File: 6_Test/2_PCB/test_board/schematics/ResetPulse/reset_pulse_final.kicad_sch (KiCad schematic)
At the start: 3 parts

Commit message: Corrections to schematic 11_20_24
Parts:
- U?: footprint D14 -> nor_gate:nor_gate_D14
- U?: value SN74HC74DR -> D_FF
- gave numbers to parts that had none: 1
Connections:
- net GND: now also U?.10 (L), U?.4 (K), U?.5 (C), U?.6 (D), U?.8 (E), U?.9 (F)
- net V_SUP: now also U?.1 (*1CLR), U?.10 (*2PRE), U?.13 (*2CLR), U?.4 (*1PRE)
- net at U?.3 (J): now also U?.11 (2CLK); no longer U?.12 (2D)
- net at U?.5 (1Q): now also U?.12 (2D)

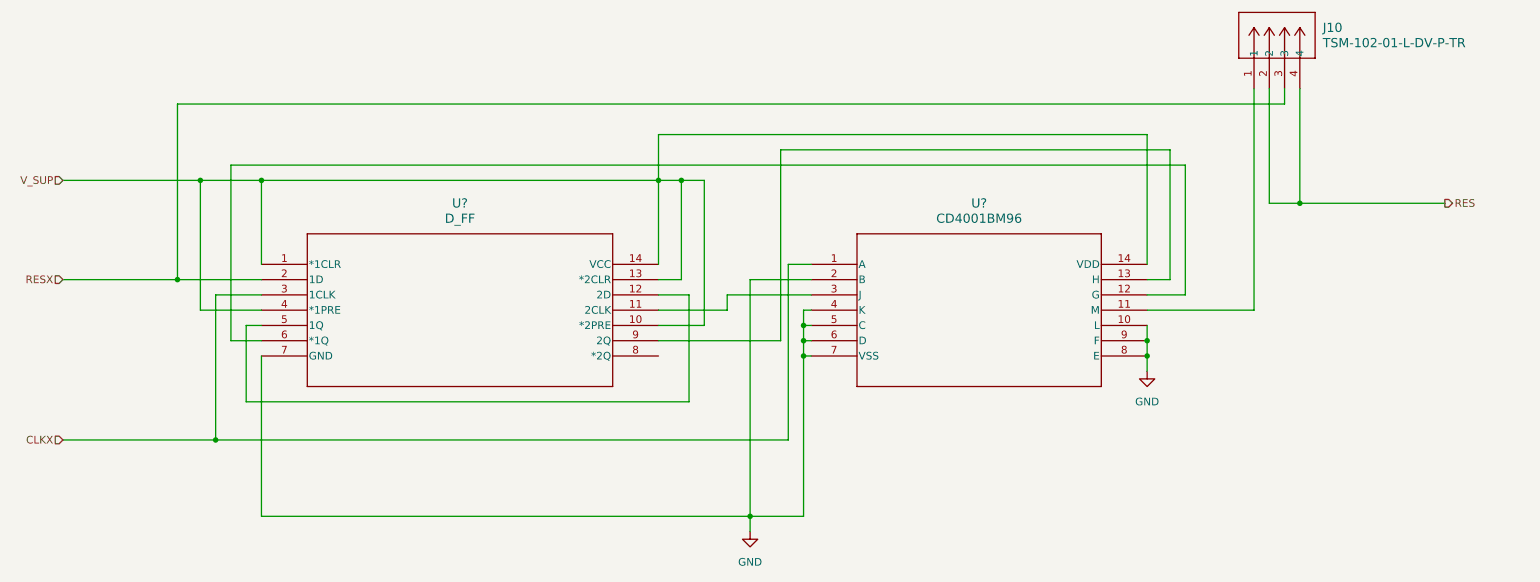
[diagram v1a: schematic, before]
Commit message: Revert "Corrections to schematic 11_20_24"
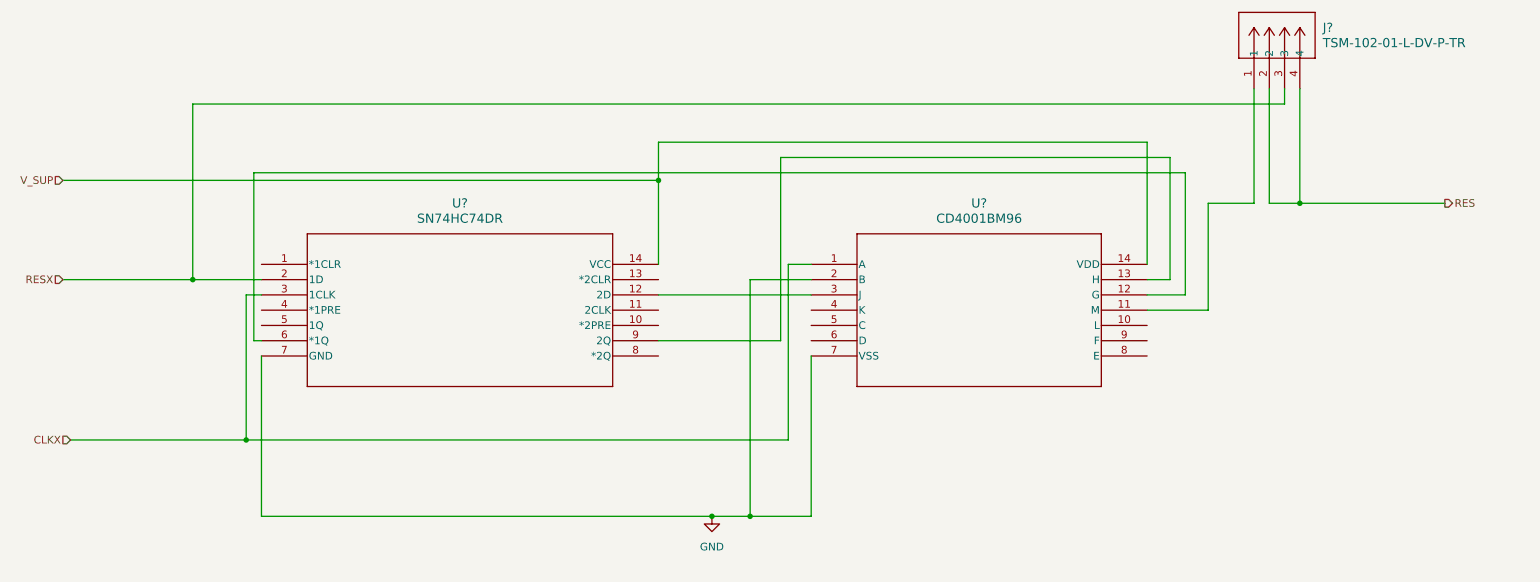
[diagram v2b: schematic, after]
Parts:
- U?: footprint nor_gate:nor_gate_D14 -> D14
- U?: value D_FF -> SN74HC74DR
- renumbered J10 to J?
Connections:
- net GND: no longer U?.10 (L), U?.4 (K), U?.5 (C), U?.6 (D), U?.8 (E), U?.9 (F)
- net V_SUP: no longer U?.1 (*1CLR), U?.10 (*2PRE), U?.13 (*2CLR), U?.4 (*1PRE)
- net at U?.3 (J): now also U?.12 (2D); no longer U?.11 (2CLK)
- net at U?.5 (1Q): no longer U?.12 (2D)
